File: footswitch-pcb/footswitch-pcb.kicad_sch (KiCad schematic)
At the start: 14 parts, among them Q1 BUK7880-55A, U1 SeeeduinoXIAO

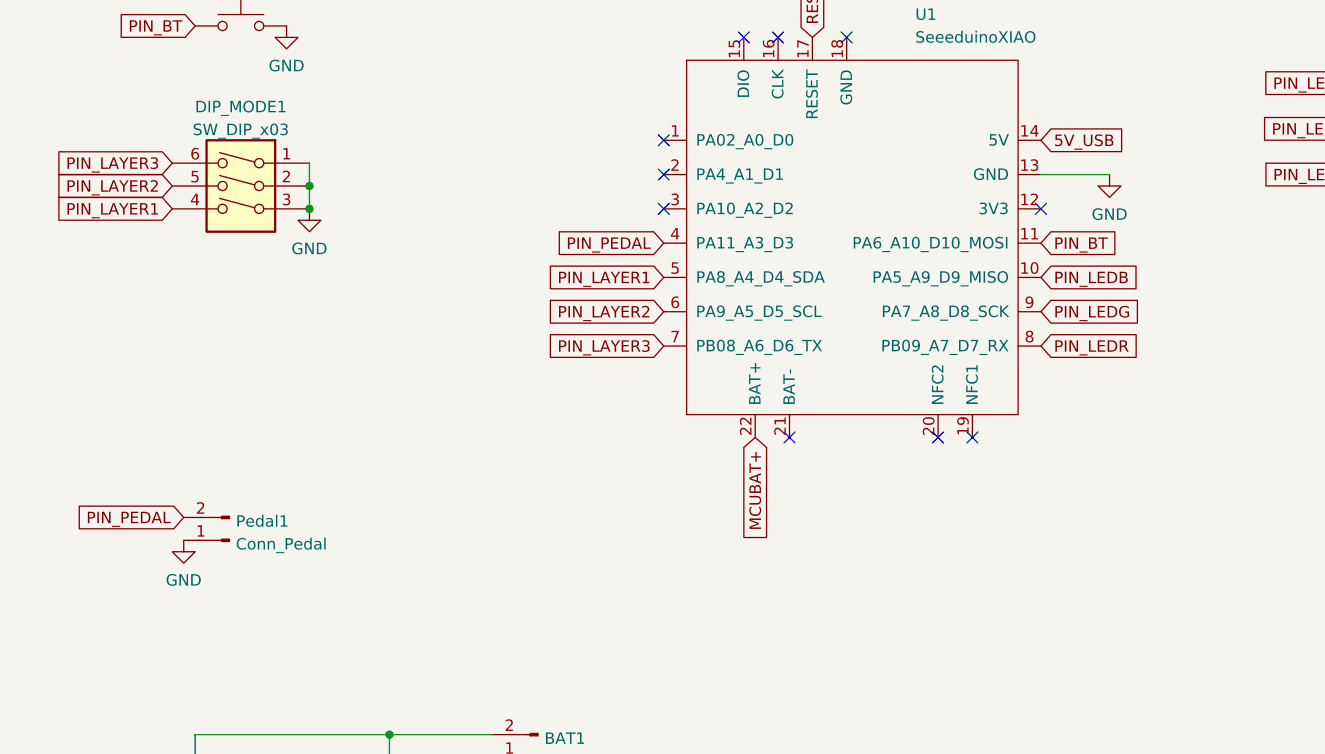
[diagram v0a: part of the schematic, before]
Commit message: Onboard Cherry Switch
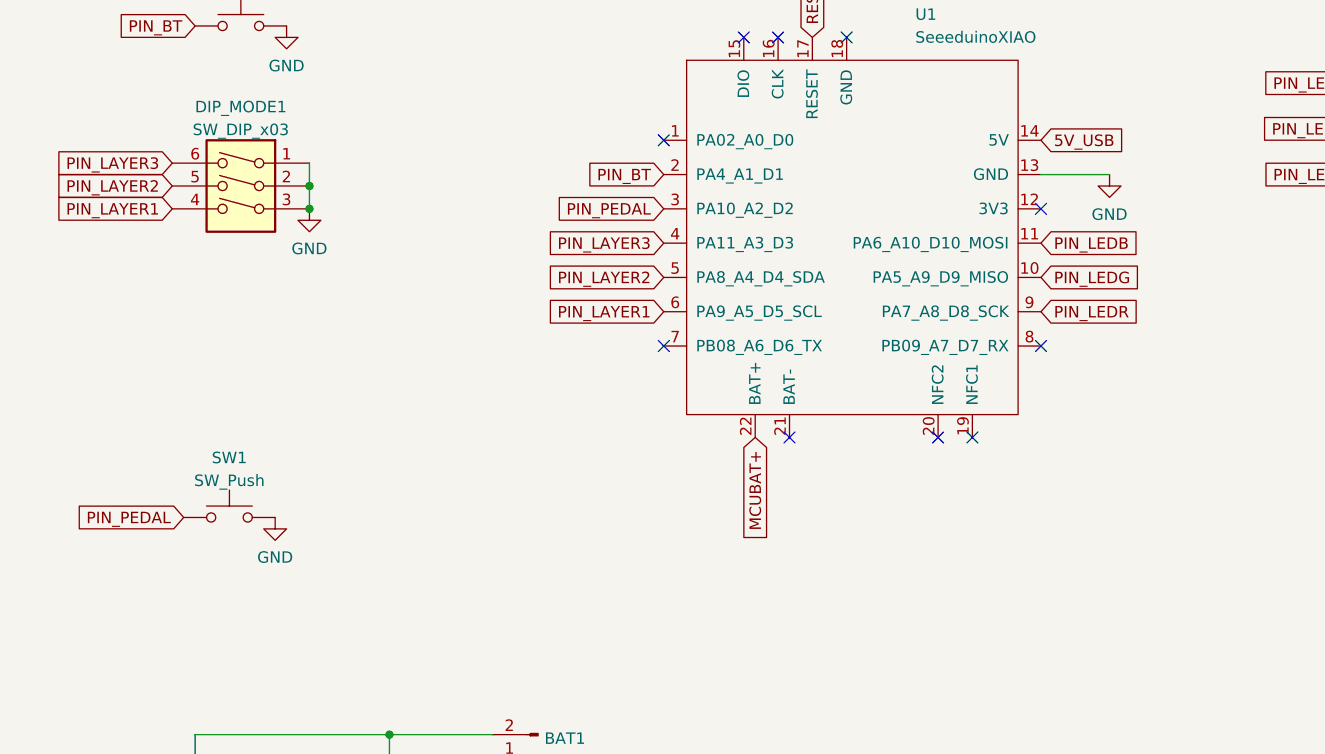
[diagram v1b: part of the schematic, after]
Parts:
- removed Pedal1: Conn_Pedal, Connector_PinHeader_2.54mm:PinHeader_1x02_P2.54mm_Horizontal, symbol Connector:Conn_01x02_Male
- added SW1: SW_Push, Button_Switch_Keyboard:SW_Cherry_MX_1.00u_PCB, symbol Switch:SW_Push
- Q1: footprint (none) -> Package_TO_SOT_SMD:SOT-23
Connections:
- net GND: now also SW1.2
- net PIN_BT: now also U1.2 (PA4_A1_D1); no longer U1.11 (PA6_A10_D10_MOSI)
- net PIN_LAYER1: now also U1.6 (PA9_A5_D5_SCL); no longer U1.5 (PA8_A4_D4_SDA)
- net PIN_LAYER2: now also U1.5 (PA8_A4_D4_SDA); no longer U1.6 (PA9_A5_D5_SCL)
- net PIN_LAYER3: now also U1.4 (PA11_A3_D3); no longer U1.7 (PB08_A6_D6_TX)
- net PIN_LEDB: now also U1.11 (PA6_A10_D10_MOSI); no longer U1.10 (PA5_A9_D9_MISO)
- net PIN_LEDG: now also U1.10 (PA5_A9_D9_MISO); no longer U1.9 (PA7_A8_D8_SCK)
- net PIN_LEDR: now also U1.9 (PA7_A8_D8_SCK); no longer U1.8 (PB09_A7_D7_RX)
- net PIN_PEDAL: now also U1.3 (PA10_A2_D2), SW1.1; no longer U1.4 (PA11_A3_D3)
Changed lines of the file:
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@@
   (no_connect (at 152.4 74.93))
   (no_connect (at 124.46 100.33))
+  (no_connect (at 110.49 90.17))
   (no_connect (at 144.78 100.33))
   (no_connect (at 140.97 100.33))
@@
   (no_connect (at 130.81 55.88))
   (no_connect (at 110.49 67.31))
-  (no_connect (at 110.49 71.12))
-  (no_connect (at 110.49 74.93))
+  (no_connect (at 152.4 90.17))
   (wire (pts (xy 58.42 133.35) (xy 58.42 139.7))
     (stroke (width 0) (type default) (color 0 0 0 0))
@@
     (effects (font (size 1.27 1.27)) (justify left bottom))
   )
-  (global_label "PIN_PEDAL" (shape input) (at 110.49 78.74 180) (fields_autoplaced)
-    (effects (font (size 1.27 1.27)) (justify right))
-    (property "Intersheet References" "${INTERSHEET_REFS}" (id 0) (at 98.0983 78.6606 0)
+  (global_label "PIN_PEDAL" (shape input) (at 110.49 74.93 180) (fields_autoplaced)
+    (effects (font (size 1.27 1.27)) (justify right))
+    (property "Intersheet References" "${INTERSHEET_REFS}" (id 0) (at 98.0983 74.8506 0)
       (effects (font (size 1.27 1.27)) (justify right) hide)
     )
@@
     )
   )
-  (global_label "PIN_LEDR" (shape input) (at 152.4 90.17 0) (fields_autoplaced)
+  (global_label "PIN_LEDR" (shape input) (at 152.4 86.36 0) (fields_autoplaced)
     (effects (font (size 1.27 1.27)) (justify left))
-    (property "Intersheet References" "${INTERSHEET_REFS}" (id 0) (at 163.7031 90.2494 0)
+    (property "Intersheet References" "${INTERSHEET_REFS}" (id 0) (at 163.7031 86.4394 0)
       (effects (font (size 1.27 1.27)) (justify left) hide)
     )
@@
     )
   )
-  (global_label "PIN_LAYER1" (shape input) (at 110.49 82.55 180) (fields_autoplaced)
-    (effects (font (size 1.27 1.27)) (justify right))
-    (property "Intersheet References" "${INTERSHEET_REFS}" (id 0) (at 97.0702 82.6294 0)
+  (global_label "PIN_LAYER1" (shape input) (at 110.49 86.36 180) (fields_autoplaced)
+    (effects (font (size 1.27 1.27)) (justify right))
+    (property "Intersheet References" "${INTERSHEET_REFS}" (id 0) (at 97.0702 86.2806 0)
       (effects (font (size 1.27 1.27)) (justify right) hide)
     )
@@
     )
   )
-  (global_label "PIN_LAYER2" (shape input) (at 110.49 86.36 180) (fields_autoplaced)
-    (effects (font (size 1.27 1.27)) (justify right))
-    (property "Intersheet References" "${INTERSHEET_REFS}" (id 0) (at 97.0702 86.4394 0)
-      (effects (font (size 1.27 1.27)) (justify right) hide)
-    )
-  )
-  (global_label "PIN_LAYER3" (shape input) (at 110.49 90.17 180) (fields_autoplaced)
-    (effects (font (size 1.27 1.27)) (justify right))
-    (property "Intersheet References" "${INTERSHEET_REFS}" (id 0) (at 97.0702 90.2494 0)
+  (global_label "PIN_LAYER2" (shape input) (at 110.49 82.55 180) (fields_autoplaced)
+    (effects (font (size 1.27 1.27)) (justify right))
+    (property "Intersheet References" "${INTERSHEET_REFS}" (id 0) (at 97.0702 82.4706 0)
+      (effects (font (size 1.27 1.27)) (justify right) hide)
+    )
+  )
+  (global_label "PIN_LAYER3" (shape input) (at 110.49 78.74 180) (fields_autoplaced)
+    (effects (font (size 1.27 1.27)) (justify right))
+    (property "Intersheet References" "${INTERSHEET_REFS}" (id 0) (at 97.0702 78.6606 0)
       (effects (font (size 1.27 1.27)) (justify right) hide)
     )
@@
     )
   )
-  (global_label "PIN_BT" (shape input) (at 152.4 78.74 0) (fields_autoplaced)
-    (effects (font (size 1.27 1.27)) (justify left))
-    (property "Intersheet References" "${INTERSHEET_REFS}" (id 0) (at 161.2236 78.8194 0)
-      (effects (font (size 1.27 1.27)) (justify left) hide)
-    )
-  )
-  (global_label "PIN_LEDG" (shape input) (at 152.4 86.36 0) (fields_autoplaced)
-    (effects (font (size 1.27 1.27)) (justify left))
-    (property "Intersheet References" "${INTERSHEET_REFS}" (id 0) (at 163.7031 86.4394 0)
-      (effects (font (size 1.27 1.27)) (justify left) hide)
-    )
-  )
-  (global_label "PIN_LEDB" (shape input) (at 152.4 82.55 0) (fields_autoplaced)
+  (global_label "PIN_BT" (shape input) (at 110.49 71.12 180) (fields_autoplaced)
+    (effects (font (size 1.27 1.27)) (justify right))
+    (property "Intersheet References" "${INTERSHEET_REFS}" (id 0) (at 101.6664 71.0406 0)
+      (effects (font (size 1.27 1.27)) (justify right) hide)
+    )
+  )
+  (global_label "PIN_LEDG" (shape input) (at 152.4 82.55 0) (fields_autoplaced)
     (effects (font (size 1.27 1.27)) (justify left))
     (property "Intersheet References" "${INTERSHEET_REFS}" (id 0) (at 163.7031 82.6294 0)
+      (effects (font (size 1.27 1.27)) (justify left) hide)
+    )
+  )
+  (global_label "PIN_LEDB" (shape input) (at 152.4 78.74 0) (fields_autoplaced)
+    (effects (font (size 1.27 1.27)) (justify left))
+    (property "Intersheet References" "${INTERSHEET_REFS}" (id 0) (at 163.7031 78.8194 0)
       (effects (font (size 1.27 1.27)) (justify left) hide)
     )
@@
     (pin "3")
   )
-  (symbol (lib_name "Conn_01x02_Male_2") (lib_id "Connector:Conn_01x02_Male") (at 62.23 111.76 180) (unit 1)
-    (in_bom yes) (on_board yes) (fields_autoplaced)
-    (property "Reference" "Pedal1" (id 0) (at 62.9412 109.6553 0)
-      (effects (font (size 1.27 1.27)) (justify right))
-    )
-    (property "Value" "Conn_Pedal" (id 1) (at 62.9412 112.1922 0)
-      (effects (font (size 1.27 1.27)) (justify right))
-    )
-    (property "Footprint" "Connector_PinHeader_2.54mm:PinHeader_1x02_P2.54mm_Horizontal" (id 2) (at 62.23 111.76 0)
-      (effects (font (size 1.27 1.27)) hide)
-    )
-    (property "Datasheet" "~" (id 3) (at 62.23 111.76 0)
-      (effects (font (size 1.27 1.27)) hide)
-    )
-    (pin "1")
-    (pin "2")
-  )
   (symbol (lib_id "power:GND") (at 210.82 66.04 0) (unit 1)
     (in_bom yes) (on_board yes) (fields_autoplaced)
@@
       (effects (font (size 1.27 1.27)) (justify left))
     )
-    (property "Footprint" "" (id 2) (at 60.96 146.685 0)
+    (property "Footprint" "Package_TO_SOT_SMD:SOT-23" (id 2) (at 60.96 146.685 0)
       (effects (font (size 1.27 1.27) italic) (justify left) hide)
     )
@@
   (symbol (lib_id "power:GND") (at 71.12 74.93 0) (unit 1)
     (in_bom yes) (on_board yes) (fields_autoplaced)
-    (property "Reference" "#PWR?" (id 0) (at 71.12 81.28 0)
+    (property "Reference" "#PWR0107" (id 0) (at 71.12 81.28 0)
       (effects (font (size 1.27 1.27)) hide)
     )
@@
     )
     (pin "1")
+  )
+  (symbol (lib_id "Switch:SW_Push") (at 62.23 109.22 0) (unit 1)
+    (in_bom yes) (on_board yes) (fields_autoplaced)
+    (property "Reference" "SW1" (id 0) (at 62.23 102.5992 0))
+    (property "Value" "SW_Push" (id 1) (at 62.23 105.1361 0))
+    (property "Footprint" "Button_Switch_Keyboard:SW_Cherry_MX_1.00u_PCB" (id 2) (at 62.23 104.14 0)
+      (effects (font (size 1.27 1.27)) hide)
+    )
+    (property "Datasheet" "~" (id 3) (at 62.23 104.14 0)
+      (effects (font (size 1.27 1.27)) hide)
+    )
+    (pin "1")
+    (pin "2")
   )
   (symbol (lib_id "Device:R") (at 191.77 71.12 270) (unit 1)
@@
     (pin "4")
   )
-  (symbol (lib_id "power:GND") (at 57.15 111.76 0) (unit 1)
-    (in_bom yes) (on_board yes) (fields_autoplaced)
-    (property "Reference" "#PWR0106" (id 0) (at 57.15 118.11 0)
-      (effects (font (size 1.27 1.27)) hide)
-    )
-    (property "Value" "GND" (id 1) (at 57.15 116.2034 0))
-    (property "Footprint" "" (id 2) (at 57.15 111.76 0)
-      (effects (font (size 1.27 1.27)) hide)
-    )
-    (property "Datasheet" "" (id 3) (at 57.15 111.76 0)
+  (symbol (lib_id "power:GND") (at 67.31 109.22 0) (unit 1)
+    (in_bom yes) (on_board yes) (fields_autoplaced)
+    (property "Reference" "#PWR0106" (id 0) (at 67.31 115.57 0)
+      (effects (font (size 1.27 1.27)) hide)
+    )
+    (property "Value" "GND" (id 1) (at 67.31 113.6634 0))
+    (property "Footprint" "" (id 2) (at 67.31 109.22 0)
+      (effects (font (size 1.27 1.27)) hide)
+    )
+    (property "Datasheet" "" (id 3) (at 67.31 109.22 0)
       (effects (font (size 1.27 1.27)) hide)
     )
@@
       (reference "#PWR0106") (unit 1) (value "GND") (footprint "")
     )
+    (path "/7fd742a2-c19d-49cd-b12b-1a35ee4c1ba5"
+      (reference "#PWR0107") (unit 1) (value "GND") (footprint "")
+    )
     (path "/f9f6177d-17c7-40c7-8aab-eaf03b6dea45"
       (reference "#PWR0108") (unit 1) (value "GND") (footprint "")
     )
-    (path "/7fd742a2-c19d-49cd-b12b-1a35ee4c1ba5"
-      (reference "#PWR?") (unit 1) (value "GND") (footprint "")
-    )
     (path "/b7bb8517-00b5-4caf-8c18-eda7de5afdde"
       (reference "B1") (unit 1) (value "R") (footprint "Resistor_SMD:R_1206_3216Metric_Pad1.30x1.75mm_HandSolder")
@@
       (reference "G1") (unit 1) (value "R") (footprint "Resistor_SMD:R_1206_3216Metric_Pad1.30x1.75mm_HandSolder")
     )
-    (path "/2dfbc12a-2aaa-446d-bdb3-48a28cd36745"
-      (reference "Pedal1") (unit 1) (value "Conn_Pedal") (footprint "Connector_PinHeader_2.54mm:PinHeader_1x02_P2.54mm_Horizontal")
-    )
     (path "/6d7c23f0-27c3-4fa6-89cc-f79a540be70c"
       (reference "Q1") (unit 1) (value "BUK7880-55A") (footprint "Package_TO_SOT_SMD:SOT-23")
@@
       (reference "R3") (unit 1) (value "10k") (footprint "Resistor_SMD:R_1206_3216Metric_Pad1.30x1.75mm_HandSolder")
     )
+    (path "/b39d2cf3-2d13-4a7a-8d39-e0f357e39fb5"
+      (reference "SW1") (unit 1) (value "SW_Push") (footprint "Button_Switch_Keyboard:SW_Cherry_MX_1.00u_PCB")
+    )
     (path "/1dae53b3-dac4-44f9-bd0e-c8caabe3abc3"

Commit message: Small cosmetic changes
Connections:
- net 5V_USB: now also R2.1; no longer R2.2
- net GND: now also R3.2; no longer R3.1
- new net: Q1.1 (G), R2.2, R3.1
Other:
- moved on the sheet: R2, R3
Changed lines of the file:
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@@
     (pin "2")
   )
-  (symbol (lib_id "Device:R") (at 48.26 151.13 180) (unit 1)
+  (symbol (lib_id "Device:R") (at 48.26 151.13 0) (mirror y) (unit 1)
     (in_bom yes) (on_board yes)
-    (property "Reference" "R3" (id 0) (at 49.53 149.86 0)
+    (property "Reference" "R3" (id 0) (at 49.53 152.4 0)
       (effects (font (size 1.27 1.27)) (justify right))
     )
-    (property "Value" "10k" (id 1) (at 49.53 152.4 0)
+    (property "Value" "10k" (id 1) (at 49.53 149.86 0)
       (effects (font (size 1.27 1.27)) (justify right))
     )
@@
     (pin "2")
   )
-  (symbol (lib_id "Device:R") (at 44.45 144.78 270) (mirror x) (unit 1)
+  (symbol (lib_id "Device:R") (at 44.45 144.78 90) (unit 1)
     (in_bom yes) (on_board yes)
     (property "Reference" "R2" (id 0) (at 44.45 139.7 90))

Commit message: Modified new PCB
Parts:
- BTN1: renamed from BTN_BT1; value BTN_BLUETOOTH -> BT
- BTN2: renamed from BTN_RESET1; value BTN_RESET -> RESET
- SW1: value SW_Push -> PEDAL
- SW2: renamed from SW_EN1; value SW_ENABLE -> PWR
- renumbered G1 to R2, B1 to R3, R3 to R4, R2 to R5
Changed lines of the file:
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@@
   (symbol (lib_id "Switch:SW_SPDT") (at 80.01 146.05 270) (unit 1)
     (in_bom yes) (on_board yes)
-    (property "Reference" "SW_EN1" (id 0) (at 86.6308 146.05 0))
-    (property "Value" "SW_ENABLE" (id 1) (at 84.0939 146.05 0))
+    (property "Reference" "SW2" (id 0) (at 86.6308 146.05 0))
+    (property "Value" "PWR" (id 1) (at 84.0939 146.05 0))
     (property "Footprint" "Button_Switch_THT:SW_Slide_1P2T_CK_OS102011MS2Q" (id 2) (at 80.01 146.05 0)
       (effects (font (size 1.27 1.27)) hide)
@@
   (symbol (lib_id "Switch:SW_Push") (at 63.5 38.1 0) (unit 1)
     (in_bom yes) (on_board yes) (fields_autoplaced)
-    (property "Reference" "BTN_RESET1" (id 0) (at 63.5 31.4792 0))
-    (property "Value" "BTN_RESET" (id 1) (at 63.5 34.0161 0))
+    (property "Reference" "BTN2" (id 0) (at 63.5 31.4792 0))
+    (property "Value" "RESET" (id 1) (at 63.5 34.0161 0))
     (property "Footprint" "Button_Switch_THT:SW_PUSH_6mm_H7.3mm" (id 2) (at 63.5 33.02 0)
       (effects (font (size 1.27 1.27)) hide)
@@
   (symbol (lib_id "Device:R") (at 48.26 151.13 0) (mirror y) (unit 1)
     (in_bom yes) (on_board yes)
-    (property "Reference" "R3" (id 0) (at 49.53 152.4 0)
+    (property "Reference" "R4" (id 0) (at 49.53 152.4 0)
       (effects (font (size 1.27 1.27)) (justify right))
     )
@@
   (symbol (lib_id "Device:R") (at 44.45 144.78 90) (unit 1)
     (in_bom yes) (on_board yes)
-    (property "Reference" "R2" (id 0) (at 44.45 139.7 90))
+    (property "Reference" "R5" (id 0) (at 44.45 139.7 90))
     (property "Value" "100" (id 1) (at 44.45 142.24 90))
     (property "Footprint" "Resistor_SMD:R_1206_3216Metric_Pad1.30x1.75mm_HandSolder" (id 2) (at 44.45 146.558 90)
@@
   (symbol (lib_id "Switch:SW_Push") (at 63.5 54.61 0) (unit 1)
     (in_bom yes) (on_board yes) (fields_autoplaced)
-    (property "Reference" "BTN_BT1" (id 0) (at 63.5 47.9892 0))
-    (property "Value" "BTN_BLUETOOTH" (id 1) (at 63.5 50.5261 0))
+    (property "Reference" "BTN1" (id 0) (at 63.5 47.9892 0))
+    (property "Value" "BT" (id 1) (at 63.5 50.5261 0))
     (property "Footprint" "Button_Switch_THT:SW_Tactile_SPST_Angled_PTS645Vx39-2LFS" (id 2) (at 63.5 49.53 0)
       (effects (font (size 1.27 1.27)) hide)
@@
   (symbol (lib_id "Switch:SW_Push") (at 62.23 109.22 0) (unit 1)
     (in_bom yes) (on_board yes) (fields_autoplaced)
-    (property "Reference" "SW1" (id 0) (at 62.23 102.5992 0))
-    (property "Value" "SW_Push" (id 1) (at 62.23 105.1361 0))
+    (property "Reference" "SW1" (id 0) (at 62.23 101.6 0))
+    (property "Value" "PEDAL" (id 1) (at 62.23 104.14 0))
     (property "Footprint" "Button_Switch_Keyboard:SW_Cherry_MX_1.00u_PCB" (id 2) (at 62.23 104.14 0)
       (effects (font (size 1.27 1.27)) hide)
@@
   (symbol (lib_id "Device:R") (at 191.77 71.12 270) (unit 1)
     (in_bom yes) (on_board yes)
-    (property "Reference" "B1" (id 0) (at 191.77 71.12 90))
+    (property "Reference" "R3" (id 0) (at 191.77 71.12 90))
     (property "Value" "R" (id 1) (at 191.77 68.9411 90))
     (property "Footprint" "Resistor_SMD:R_1206_3216Metric_Pad1.30x1.75mm_HandSolder" (id 2) (at 191.77 69.342 90)
@@
   (symbol (lib_id "Device:R") (at 191.77 66.04 90) (mirror x) (unit 1)
     (in_bom yes) (on_board yes)
-    (property "Reference" "G1" (id 0) (at 191.77 66.04 90))
+    (property "Reference" "R2" (id 0) (at 191.77 66.04 90))
     (property "Value" "R" (id 1) (at 191.77 63.8611 90))
     (property "Footprint" "Resistor_SMD:R_1206_3216Metric_Pad1.30x1.75mm_HandSolder" (id 2) (at 191.77 64.262 90)
@@
       (reference "#PWR0108") (unit 1) (value "GND") (footprint "")
     )
-    (path "/b7bb8517-00b5-4caf-8c18-eda7de5afdde"
-      (reference "B1") (unit 1) (value "R") (footprint "Resistor_SMD:R_1206_3216Metric_Pad1.30x1.75mm_HandSolder")
-    )
     (path "/6eb4e5f0-1898-4a31-958e-2e5a03350318"
       (reference "BAT1") (unit 1) (value "Battery Connector") (footprint "Connector_JST:JST_XH_S2B-XH-A-1_1x02_P2.50mm_Horizontal")
     )
     (path "/3b9882c8-9aa0-4b87-a78a-16d5db2117c4"
-      (reference "BTN_BT1") (unit 1) (value "BTN_BLUETOOTH") (footprint "Button_Switch_THT:SW_Tactile_SPST_Angled_PTS645Vx39-2LFS")
+      (reference "BTN1") (unit 1) (value "BT") (footprint "Button_Switch_THT:SW_Tactile_SPST_Angled_PTS645Vx39-2LFS")
     )
     (path "/38af1a5b-40ba-49ed-8086-d7b128177d98"
-      (reference "BTN_RESET1") (unit 1) (value "BTN_RESET") (footprint "Button_Switch_THT:SW_PUSH_6mm_H7.3mm")
+      (reference "BTN2") (unit 1) (value "RESET") (footprint "Button_Switch_THT:SW_PUSH_6mm_H7.3mm")
     )
     (path "/e2980494-286b-4082-b45d-c732efc68e2d"
@@
       (reference "DIP_MODE1") (unit 1) (value "SW_DIP_x03") (footprint "Button_Switch_THT:SW_DIP_SPSTx03_Slide_6.7x9.18mm_W7.62mm_P2.54mm_LowProfile")
     )
-    (path "/bfd987b2-b471-4edd-9a20-44eb2e980ca7"
-      (reference "G1") (unit 1) (value "R") (footprint "Resistor_SMD:R_1206_3216Metric_Pad1.30x1.75mm_HandSolder")
-    )
     (path "/6d7c23f0-27c3-4fa6-89cc-f79a540be70c"
       (reference "Q1") (unit 1) (value "BUK7880-55A") (footprint "Package_TO_SOT_SMD:SOT-23")
@@
       (reference "R1") (unit 1) (value "R") (footprint "Resistor_SMD:R_1206_3216Metric_Pad1.30x1.75mm_HandSolder")
     )
+    (path "/bfd987b2-b471-4edd-9a20-44eb2e980ca7"
+      (reference "R2") (unit 1) (value "R") (footprint "Resistor_SMD:R_1206_3216Metric_Pad1.30x1.75mm_HandSolder")
+    )
+    (path "/b7bb8517-00b5-4caf-8c18-eda7de5afdde"
+      (reference "R3") (unit 1) (value "R") (footprint "Resistor_SMD:R_1206_3216Metric_Pad1.30x1.75mm_HandSolder")
+    )
+    (path "/3b1dc44c-db64-47a9-afdd-0c59a9191aac"
+      (reference "R4") (unit 1) (value "10k") (footprint "Resistor_SMD:R_1206_3216Metric_Pad1.30x1.75mm_HandSolder")
+    )
     (path "/3b40bec6-88fb-47a7-acdd-0e7fc95b021c"
-      (reference "R2") (unit 1) (value "100") (footprint "Resistor_SMD:R_1206_3216Metric_Pad1.30x1.75mm_HandSolder")
-    )
-    (path "/3b1dc44c-db64-47a9-afdd-0c59a9191aac"
-      (reference "R3") (unit 1) (value "10k") (footprint "Resistor_SMD:R_1206_3216Metric_Pad1.30x1.75mm_HandSolder")
+      (reference "R5") (unit 1) (value "100") (footprint "Resistor_SMD:R_1206_3216Metric_Pad1.30x1.75mm_HandSolder")
     )
     (path "/b39d2cf3-2d13-4a7a-8d39-e0f357e39fb5"
-      (reference "SW1") (unit 1) (value "SW_Push") (footprint "Button_Switch_Keyboard:SW_Cherry_MX_1.00u_PCB")
+      (reference "SW1") (unit 1) (value "PEDAL") (footprint "Button_Switch_Keyboard:SW_Cherry_MX_1.00u_PCB")
     )
     (path "/1dae53b3-dac4-44f9-bd0e-c8caabe3abc3"
-      (reference "SW_EN1") (unit 1) (value "SW_ENABLE") (footprint "Button_Switch_THT:SW_Slide_1P2T_CK_OS102011MS2Q")
+      (reference "SW2") (unit 1) (value "PWR") (footprint "Button_Switch_THT:SW_Slide_1P2T_CK_OS102011MS2Q")
     )
     (path "/1d6bc926-0438-4b17-a675-0536bdc82233"
